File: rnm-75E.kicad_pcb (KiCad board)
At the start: 2 copper layers, 323.8 x 114.3 mm, 218 parts, among them J1 AVR-ISP-6, J2 USB_C_Receptacle_USB2.0, J3 Conn_01x04, SW1 SW_Push, SW2 Rotary_Encoder_Switch, U1 AT90USB646-AU, Y1 Crystal_GND24_Small

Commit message: routing changes
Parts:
- J1: footprint Connector_PinSocket_1.00mm:PinSocket_2x03_P1.00mm_Vertical_SMD -> random_keyboard_parts:Reset_Pretty-Mask
- moved J1 307.3 mm to (357.2, 96.2), turned to 0 degrees
- moved CAPS_LOCK_LED2 289.6 mm to (382.5, 99.7)
- moved CF3 289.6 mm to (265.2, 185.4)
- moved C_F1 289.6 mm to (237.1, 180.6)
- moved C_F2 289.6 mm to (229.8, 198.9)
- moved C_FM1 289.6 mm to (237.1, 178.6)
- moved C_X1 289.6 mm to (255.5, 193.8)
- moved C_X2 289.6 mm to (255.5, 188.1)
- moved D1 289.6 mm to (78.5, 119.5)
- moved D11 289.6 mm to (103.1, 191.6)
- moved D14 289.6 mm to (129.8, 191.3)
- moved D15 289.6 mm to (126.1, 138.6)
- moved D16 289.6 mm to (130.9, 157.6)
- moved D2 289.6 mm to (78.5, 138.6)
- moved D20 289.6 mm to (150.1, 191.9)
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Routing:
- net GND: track 1174.7 -> 1295.3 mm, vias 6 -> 11
- net MISO: track 185.2 -> 206.9 mm, vias 0 -> 1
- net +5V: track 1011.6 -> 1029.7 mm
- net SCK: track 189.6 -> 204.1 mm, vias 0 -> 1
- net MOSI: track 190.1 -> 202.7 mm, vias 2 -> 1
- net RESET: track 246.7 -> 257.1 mm, vias 0 -> 1
- net Net-(D90-Pad4): track 74.2 -> 78.3 mm
- net Net-(D89-Pad4): track 71.8 -> 75.1 mm
- net VCC: track 60.4 -> 62.3 mm
- net ROWE: track 376.0 -> 377.0 mm
- added copper zone on F.Cu, net GND
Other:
- board size 323.8 x 114.3 mm -> 324.4 x 240.8 mm

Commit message: More stable design
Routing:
- net Net-(D94-Pad4): track 55.3 -> 53.6 mm
- net SDA: track 252.9 -> 253.4 mm
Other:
- board size 324.4 x 240.8 mm -> 323.9 x 260.4 mm

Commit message: TODO
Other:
- board size 323.9 x 260.4 mm -> 323.9 x 114.3 mm

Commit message: replacement added
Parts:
- U1: value AT90USB646-AU -> AT90USB1286-AU
- moved U1 0.09 mm to (242.8, 191.7)
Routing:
- net MISO: track 206.9 -> 205.8 mm

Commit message: wiring touch ups
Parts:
- moved U1 0.06 mm to (242.8, 191.7)
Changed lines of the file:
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@@
   )
   (module Package_QFP:TQFP-64_14x14mm_P0.8mm (layer B.Cu)
-    (at 242.8 191.65 270)
+    (at 242.83 191.7 270)
     (descr "64-Lead Plastic Thin Quad Flatpack (PF) - 14x14x1 mm Body, 2.00 mm [TQFP] (see Microchip Packaging Specification 00000049BS.pdf)")
     (tags "QFP 0.8")
@@
   (segment (start 182.499 175.387) (end 183.769 174.117) (width 0.254) (layer F.Cu) (net 120))
   (segment (start 183.769 174.117) (end 185.83275 174.117) (width 0.254) (layer F.Cu) (net 120))
-  (segment (start 185.039 201.422) (end 182.499 198.882) (width 0.254) (layer B.Cu) (net 120))
-  (segment (start 231.394 201.422) (end 185.039 201.422) (width 0.254) (layer B.Cu) (net 120))
-  (segment (start 232.664 200.152) (end 231.394 201.422) (width 0.254) (layer B.Cu) (net 120))
-  (segment (start 233.42525 197.73825) (end 232.664 198.4995) (width 0.254) (layer B.Cu) (net 120))
-  (segment (start 232.664 198.4995) (end 232.664 200.152) (width 0.254) (layer B.Cu) (net 120))
-  (segment (start 235.124 197.73825) (end 233.42525 197.73825) (width 0.254) (layer B.Cu) (net 120))
   (segment (start 231.386934 200.787) (end 197.739 200.787) (width 0.254) (layer B.Cu) (net 121))
   (segment (start 232.20999 199.963944) (end 231.386934 200.787) (width 0.254) (layer B.Cu) (net 121))
@@
   (segment (start 131.460875 196.738875) (end 134.654979 199.932979) (width 0.254) (layer B.Cu) (net 118))
   (segment (start 132.969 193.167) (end 131.460875 194.675125) (width 0.254) (layer B.Cu) (net 118))
+  (segment (start 185.039 201.422) (end 182.499 198.882) (width 0.254) (layer B.Cu) (net 120))
+  (segment (start 231.394 201.422) (end 185.039 201.422) (width 0.254) (layer B.Cu) (net 120))
+  (segment (start 232.664 200.152) (end 231.394 201.422) (width 0.254) (layer B.Cu) (net 120))
+  (segment (start 232.664 198.4995) (end 232.664 200.152) (width 0.254) (layer B.Cu) (net 120))
+  (segment (start 233.4635 197.7) (end 232.664 198.4995) (width 0.254) (layer B.Cu) (net 120))
+  (segment (start 235.13 197.7) (end 233.4635 197.7) (width 0.254) (layer B.Cu) (net 120))
   (segment (start 223.666797 174.117) (end 223.93275 174.117) (width 0.254) (layer F.Cu) (net 122))
   (segment (start 214.40775 164.857953) (end 223.666797 174.117) (width 0.254) (layer F.Cu) (net 122))

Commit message: srv05 added
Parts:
- removed ESD1: PRTR5V0U2X, Package_TO_SOT_SMD:SOT-143
- added U2: SRV05-4, Package_TO_SOT_SMD:SOT-23-6, B.Cu at (376.6, 104.9)
- turned C_F1 to 180 degrees
- turned C_FM1 to 180 degrees
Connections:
- U1 pad 10: LED_PIN -> (no net)
- U1 pad 33: (no net) -> LED_PIN
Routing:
- net GND: track 1295.3 -> 1487.3 mm
- net +5V: track 1029.9 -> 995.8 mm, vias 12 -> 10
- net COL8: track 109.8 -> 101.4 mm
- net LED_PIN: track 270.8 -> 278.1 mm
- net D+: track 196.7 -> 200.9 mm
- net D-: track 196.4 -> 200.6 mm
- net ROWF: track 369.4 -> 372.4 mm
- net RESET: track 257.1 -> 255.8 mm
- net VCC: track 62.3 -> 62.8 mm

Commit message: update fill
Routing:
- net +5V: track 995.8 -> 1010.8 mm, vias 10 -> 11
- net GND: track 1487.3 -> 1485.7 mm

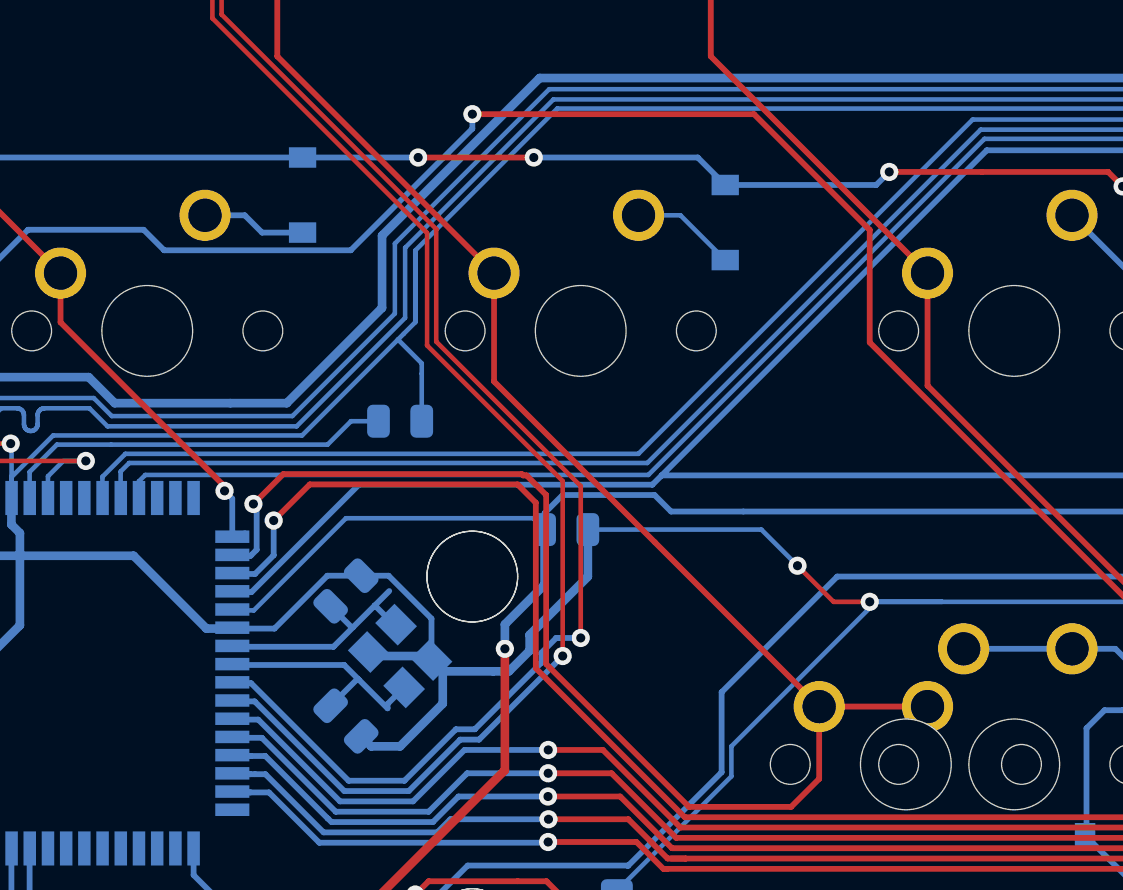
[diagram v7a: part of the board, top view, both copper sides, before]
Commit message: updated crystal position
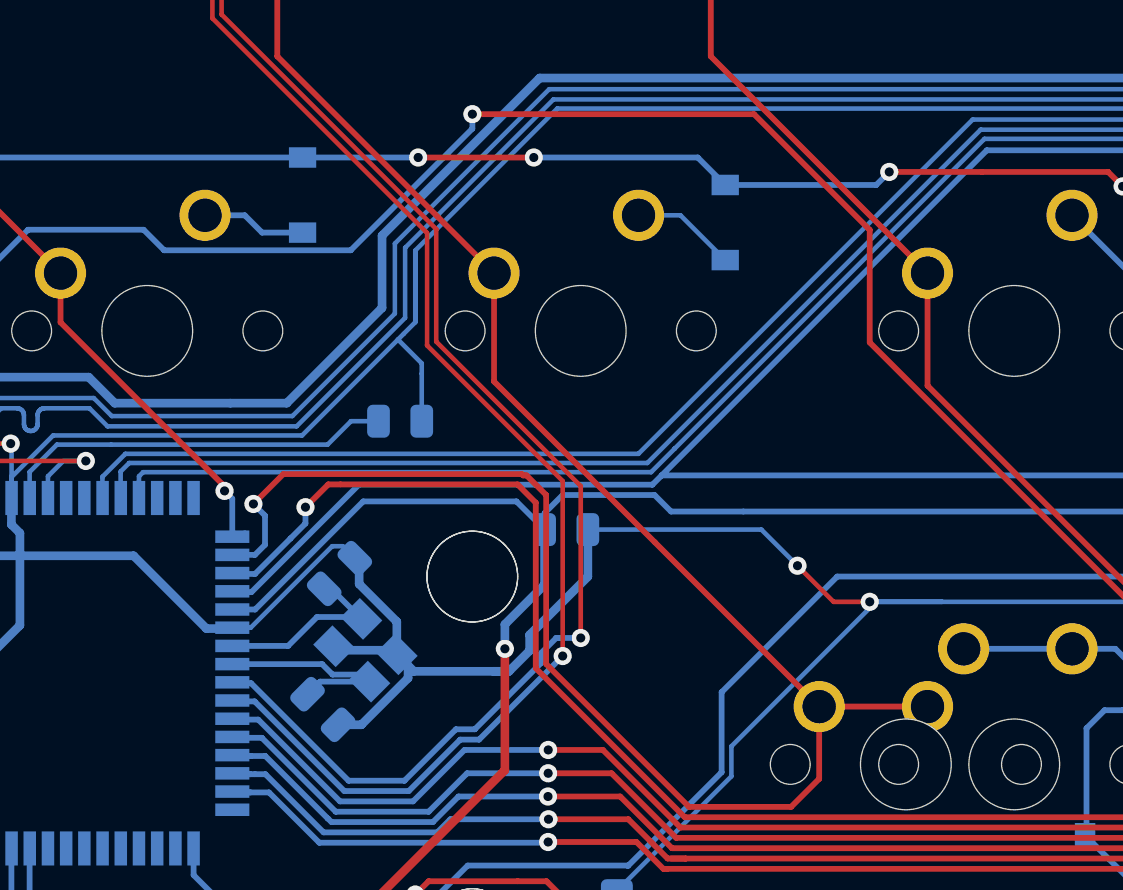
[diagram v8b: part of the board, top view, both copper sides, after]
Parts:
- moved Y1 1.55 mm to (256.4, 190.7)
- moved C_X1 1.14 mm to (254.5, 193.3)
- moved C_X2 0.82 mm to (255.2, 187.3)
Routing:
- net XTAL2: track 11.0 -> 9.30 mm
- net +5V: track 1010.8 -> 1012.1 mm
- net XTAL1: track 11.3 -> 10.0 mm
- net MISO: track 205.8 -> 206.7 mm
- net COL9: track 158.6 -> 159.4 mm
- net GND: track 1485.7 -> 1486.5 mm
